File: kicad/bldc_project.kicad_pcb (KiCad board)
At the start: 4 copper layers, 100 x 60 mm, 160 parts, among them J1 Conn_ARM_SWD_TagConnect_TC203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, J2 Screw_Terminal_01x03, J3 Screw_Terminal_01x03, J4 TYPE-C-31-M-12, Q1 IRFZ44N, Q2 IRFZ44N, Q3 IRFZ44N, Q4 IRFZ44N, Q5 IRFZ44N, Q6 IRFZ44N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

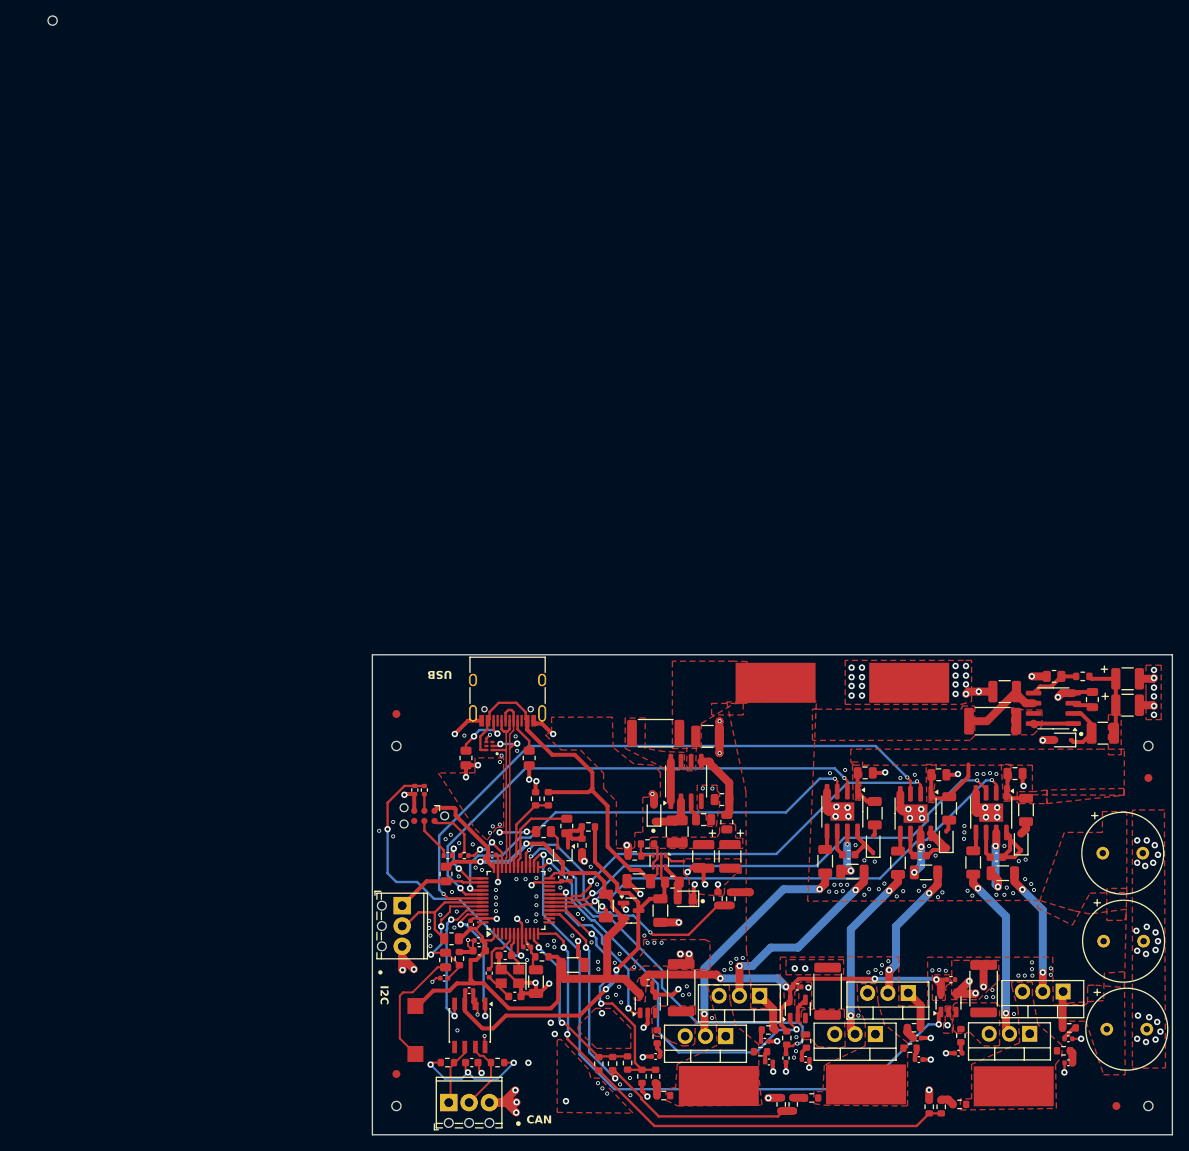
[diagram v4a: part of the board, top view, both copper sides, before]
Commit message: changed inductors, rearranged new FET footprints and symbols
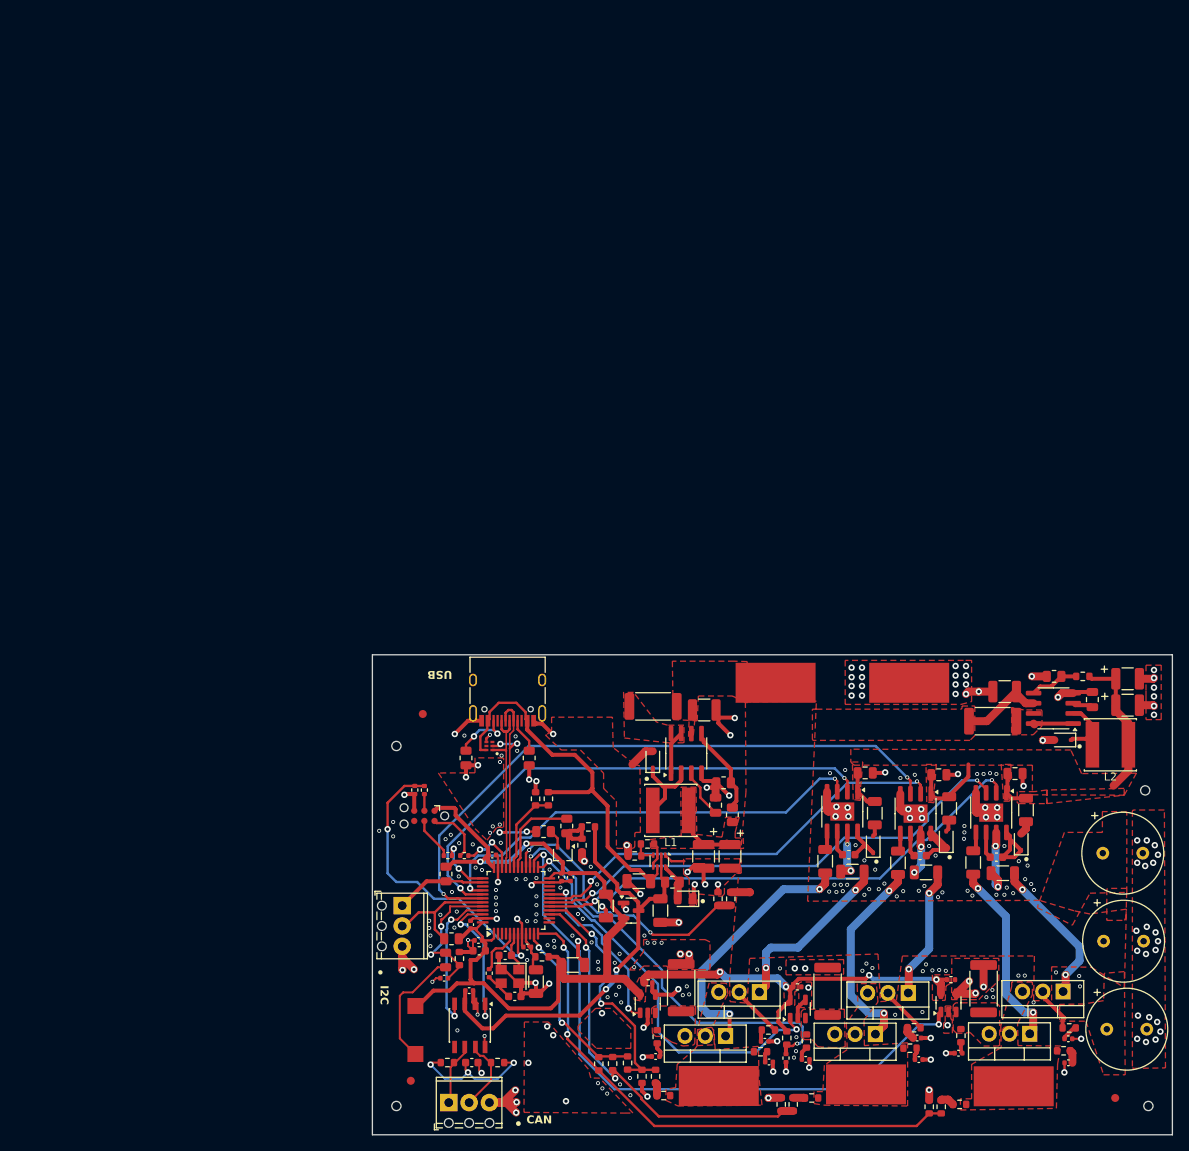
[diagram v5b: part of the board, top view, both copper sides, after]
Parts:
- removed FM4: Fiducial, Fiducial:Fiducial_1mm_Mask2mm
- removed H5: MountingHole, bldc:MountingHole_1.152mm_jlcpcb
- L1, L2: footprint Inductor_SMD:L_1210_3225Metric -> Inductor_SMD:L_Sunlord_SWPA6045S
- Q1, Q2, Q3, Q4, Q5, Q6: value IRFZ44N -> IRFZ44NPBF
- moved Q6 6.94 mm to (89.6, 122.7)
- moved D4 6.70 mm to (76.2, 93.6)
- moved Q5 6.60 mm to (85.3, 128.2)
- moved H1 5.56 mm to (137.8, 97.5)
- moved U10 3.50 mm to (80.4, 92.8)
- moved R59 3.37 mm to (76.3, 87.0)
- moved C44 3.33 mm to (82.7, 87.4)
- moved FM1 3.30 mm to (47.5, 87.9)
- moved L1 2.77 mm to (78.5, 100.0), turned to 180 degrees
- moved C42 2.34 mm to (84.1, 99.3), turned to -90 degrees
- moved R54 2.11 mm to (85.1, 96.5)
- moved FM2 1.99 mm to (46.0, 133.8)
- moved L2 1.73 mm to (133.4, 91.8)
- moved R47 1.15 mm to (86.2, 100.5)
- moved FM3 1.01 mm to (134.1, 135.9)
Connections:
- Q1 pad 1: +BATT -> Net-(Q1-G)
- Q1 pad 2: Net-(Q1-G) -> +BATT
- Q2 pad 1: /DRIVER/PhaseU -> Net-(Q2-G)
- Q2 pad 2: Net-(Q2-G) -> /DRIVER/PhaseU
- Q3 pad 1: +BATT -> Net-(Q3-G)
- Q3 pad 2: Net-(Q3-G) -> +BATT
- Q4 pad 1: /DRIVER/PhaseV -> Net-(Q4-G)
- Q4 pad 2: Net-(Q4-G) -> /DRIVER/PhaseV
- Q5 pad 1: +BATT -> Net-(Q5-G)
- Q5 pad 2: Net-(Q5-G) -> /DRIVER/PhaseW
- Q5 pad 3: /DRIVER/PhaseW -> /DRIVER/PhaseW_CURRENT+
- Q6 pad 1: /DRIVER/PhaseW -> Net-(Q6-G)
- Q6 pad 2: Net-(Q6-G) -> +BATT
- Q6 pad 3: /DRIVER/PhaseW_CURRENT+ -> /DRIVER/PhaseW
- R6 pad 2: Net-(Q5-G) -> Net-(Q6-G)
- R7 pad 2: Net-(Q6-G) -> Net-(Q5-G)
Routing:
- net GND: track 171.9 -> 181.9 mm, vias 278 -> 272
- net /POWER/VBUCK5_OUT: track 3.60 -> 11.9 mm
- net +10V: track 30.5 -> 38.4 mm
- net Net-(Q5-G): track 24.9 -> 32.6 mm
- net Net-(Q6-G): track 29.4 -> 22.5 mm
- net Net-(D4-K): track 5.30 -> 10.00 mm
- net +BATT: track 27.6 -> 31.4 mm
- net Net-(U10-TC): track 2.55 -> 6.21 mm
- net Net-(Q4-G): track 22.6 -> 25.7 mm
- net Net-(Q1-G): track 16.3 -> 19.1 mm
- net Net-(Q2-G): track 21.8 -> 23.9 mm
- net Net-(U10-Vfb): track 8.81 -> 10.7 mm
- net Net-(Q3-G): track 17.7 -> 16.7 mm
- net +3.3V: track 158.0 -> 158.9 mm
- net /DRIVER/PhaseU: track 0.00 -> 0.62 mm
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
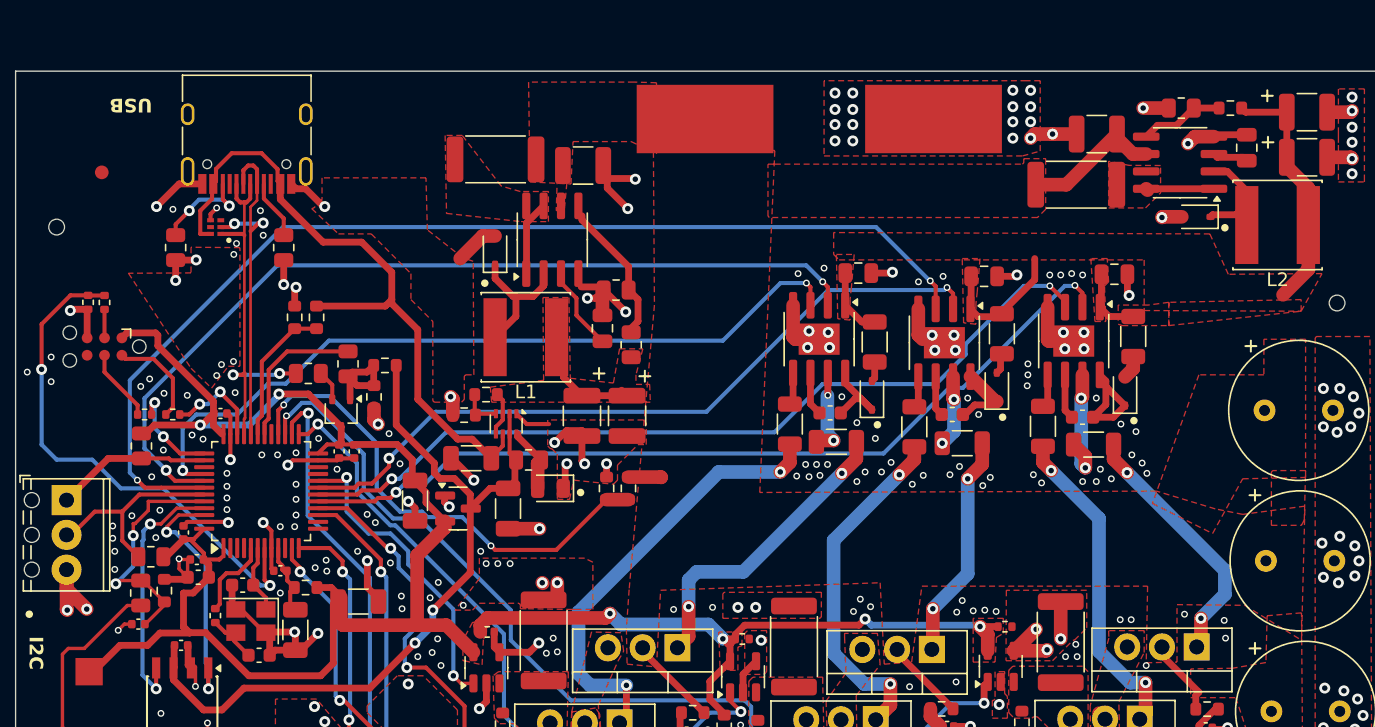
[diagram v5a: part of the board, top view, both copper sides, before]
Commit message: [kicad] Rechecked all footprints and components requirements | TODO: think about replacing the ESD package with something else [simulations] Checked simulations of buck converter with reality
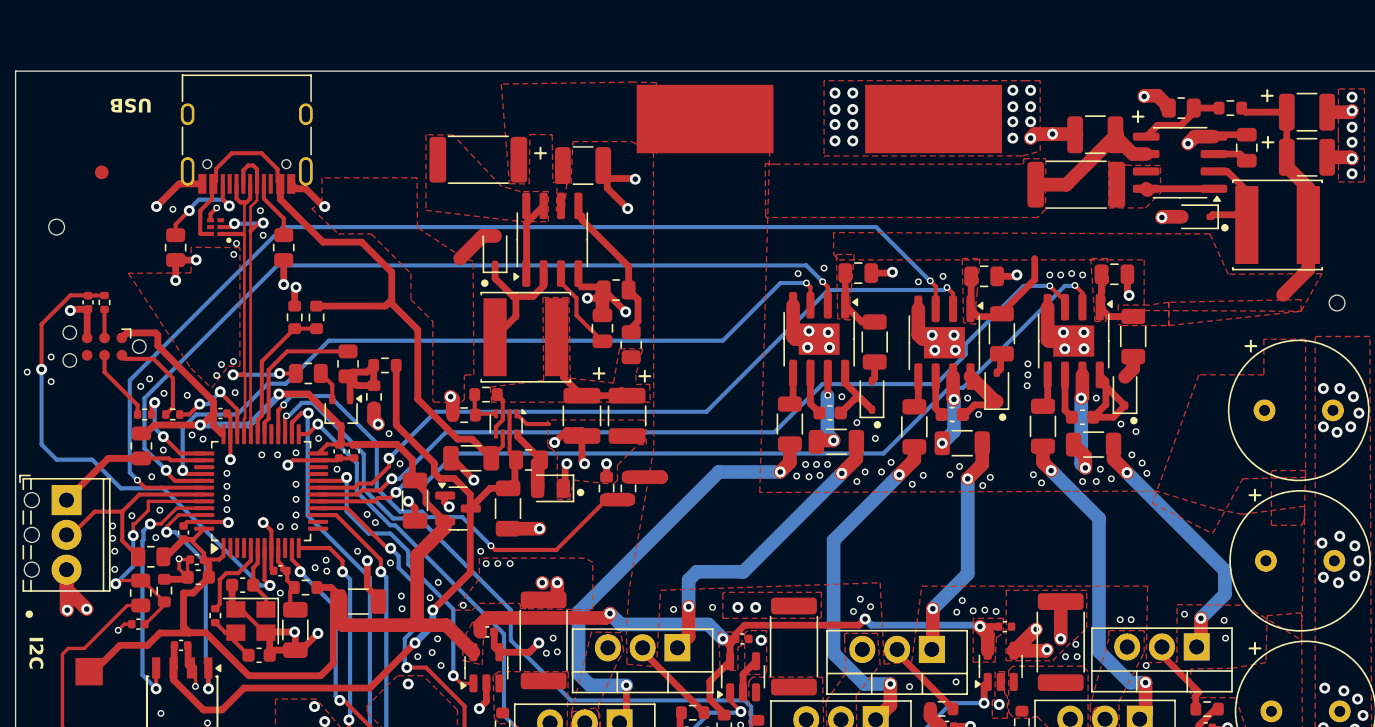
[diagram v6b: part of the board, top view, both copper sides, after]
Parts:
- C19, C20, C21, C32: footprint Resistor_SMD:R_0402_1005Metric -> Capacitor_SMD:C_0402_1005Metric
- moved R59 1.26 mm to (75.0, 87.0)
- moved C45 0.12 mm to (120.1, 85.2)

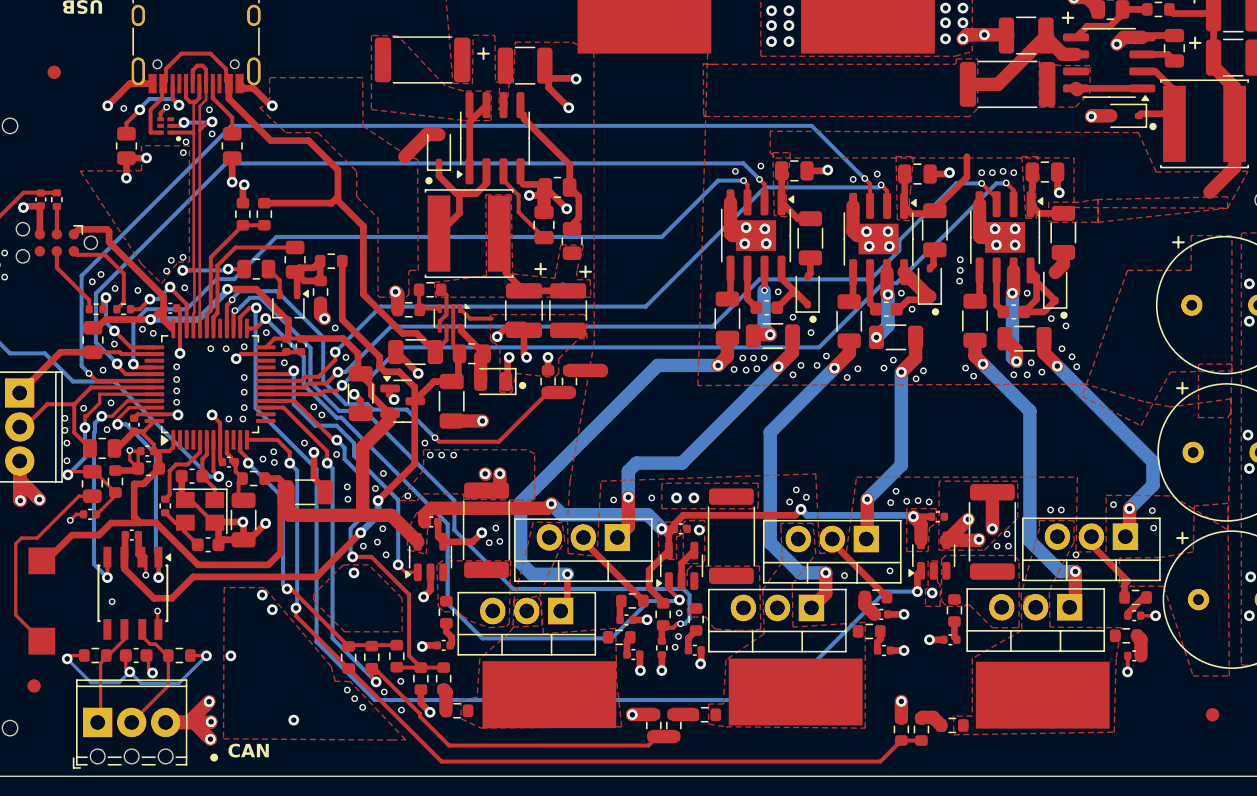
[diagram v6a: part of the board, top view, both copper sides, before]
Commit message: [kicad] Added different ESD protection device, silkscreen indication on the back, [review] Added pdf file and images of the front and back as well as 3d images
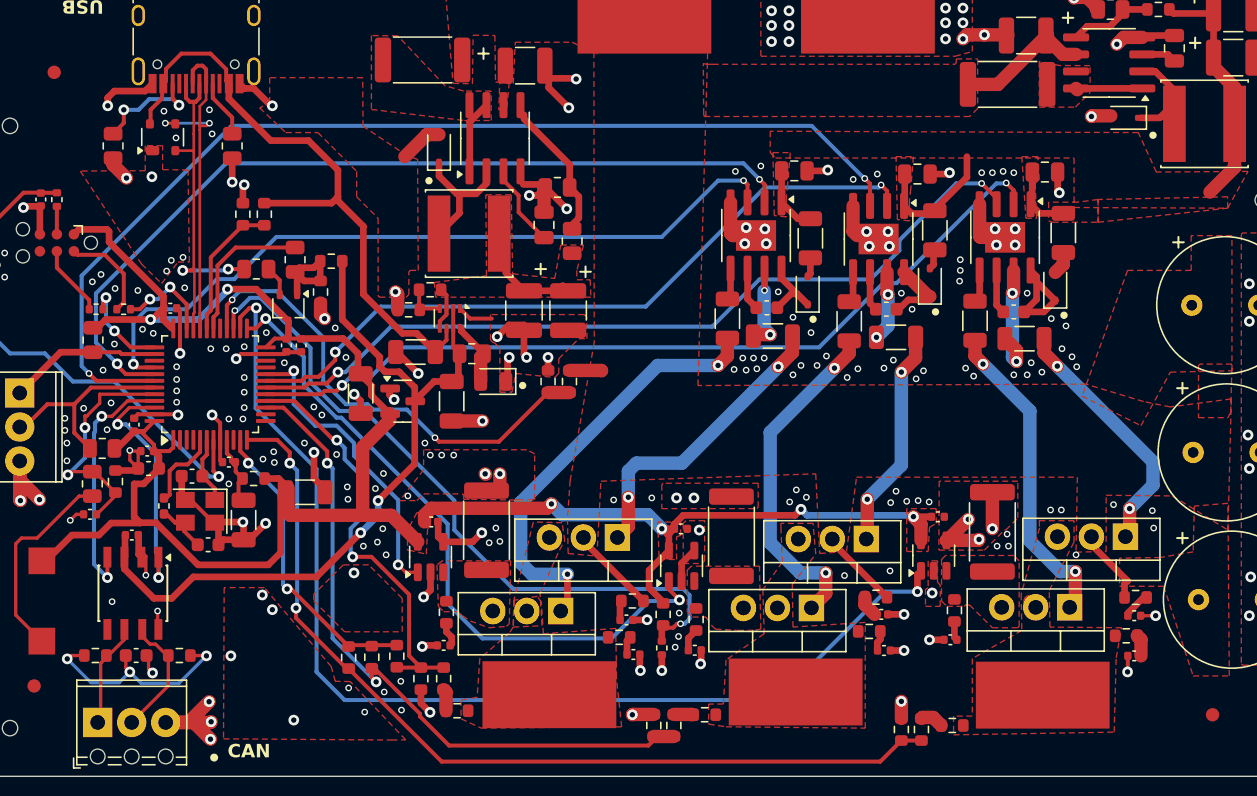
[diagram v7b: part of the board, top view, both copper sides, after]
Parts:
- removed U9: TPD4S012DRYR, bldc:TI_R-PUSON-N6
- added D7: PRTR5V0U2X,215, Package_TO_SOT_SMD:SOT-143, F.Cu at (55.6, 92.8)
- L1, L2: value 100u -> 100uH
- R45: footprint Resistor_SMD:R_0402_1005Metric -> Resistor_SMD:R_0402_1005Metric_Pad0.72x0.64mm_HandSolder
- moved R56 1.00 mm to (51.9, 93.4)
- moved D5 0.15 mm to (127.5, 91.3)
- moved R45 0.10 mm to (55.7, 120.3)
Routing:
- net GND: track 182.3 -> 180.5 mm, vias 272 -> 269
- net PhaseU_CURRENT: track 80.9 -> 82.2 mm
- net USB_VBUS: track 49.3 -> 48.0 mm
- net Net-(J4-CC2): track 7.51 -> 8.57 mm
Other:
- board text added: "10V"
- board text added: "5V"
- board text added: "BATT"
- board text added: "BLDC Driver, rev 1"
- board text added: "G"
- board text added: "GND"
- board text added: "PhaseU"
- board text added: "PhaseV"
- board text added: "PhaseW"
